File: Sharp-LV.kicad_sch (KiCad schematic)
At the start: 51 parts, among them J1 USB_C_Receptacle_USB2.0, J2 Conn_01x05_PROG, J3 5024260810, J4 FH52-10S-0.5SH_99, J5 SM04B-SRSS-TB_LF__SN_, J6 Conn_2Rows-13Pins, J7 S2B-PH-SM4-TB_LF__SN_, U1 NRF52840-QIAA-R, U2 USBLC6-2P6, U3 MCP1700-3302E_SOT23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

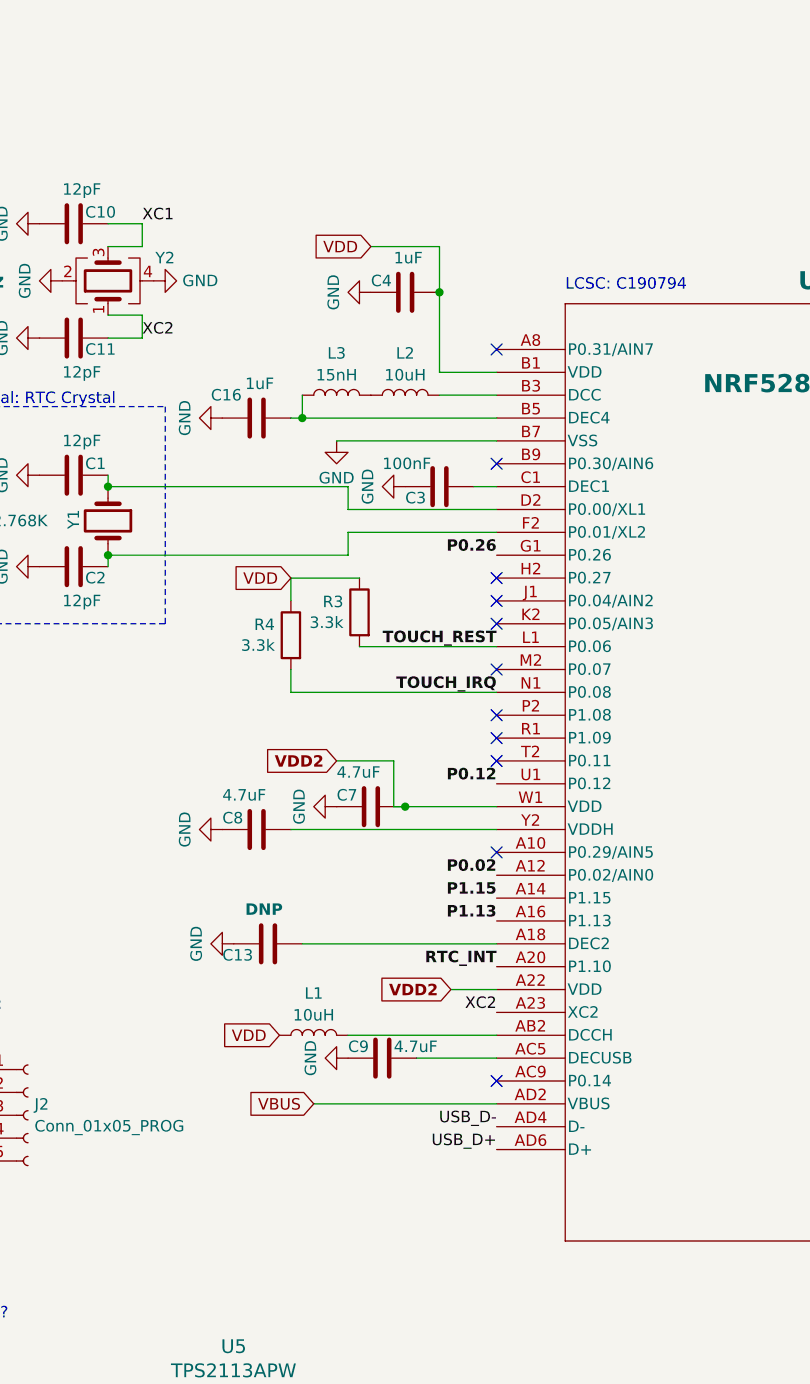
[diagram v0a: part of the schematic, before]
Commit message: Update SCH and add C22 to VUSB
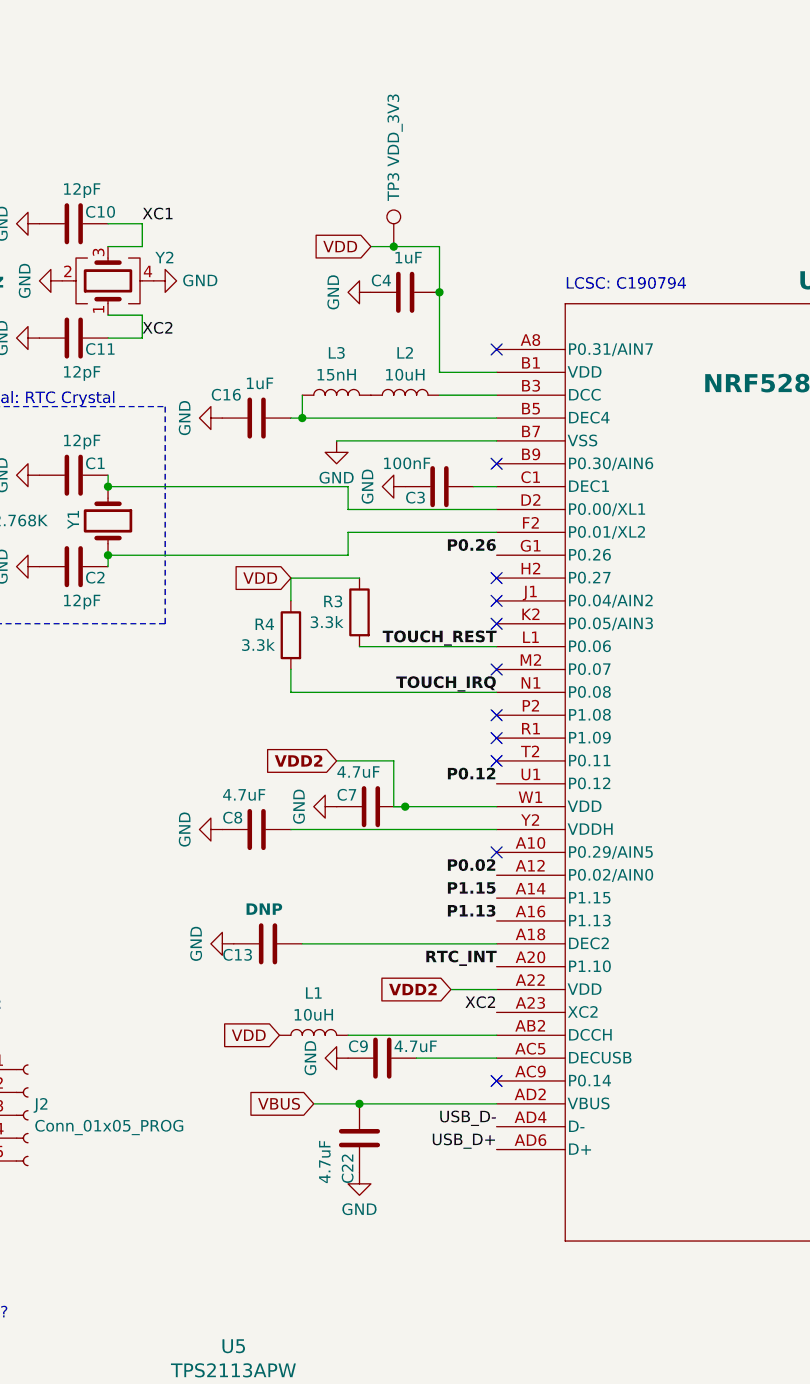
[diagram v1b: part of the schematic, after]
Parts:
- added C22: 4.7uF, Capacitor_SMD:C_0402_1005Metric, symbol Device:C
- added TP3: VDD_3V3, TestPoint:TestPoint_Pad_D1.5mm, symbol Connector:TestPoint
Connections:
- net GND: now also C22.1
- net VBUS: now also C22.2
- net VDD: now also TP3.1
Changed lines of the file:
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@@
   (junction (at 172.72 180.34) (diameter 0) (color 0 0 0 0)
   )
+  (junction (at 168.91 33.02) (diameter 0) (color 0 0 0 0)
+  )
   (junction (at 67.31 58.42) (diameter 0) (color 0 0 0 0)
   )
@@
   (junction (at 67.31 60.96) (diameter 0) (color 0 0 0 0)
   )
+  (junction (at 165.1 128.27) (diameter 0) (color 0 0 0 0)
+  )
   (junction (at 52.07 120.65) (diameter 0) (color 0 0 0 0)
   )
@@
     (stroke (width 0) (type default))
   )
-  (wire (pts (xy 160.02 128.27) (xy 180.34 128.27))
+  (wire (pts (xy 160.02 128.27) (xy 165.1 128.27))
     (stroke (width 0) (type default))
   )
@@
     (stroke (width 0) (type default))
   )
+  (wire (pts (xy 165.1 128.27) (xy 180.34 128.27))
+    (stroke (width 0) (type default))
+  )
   (wire (pts (xy 306.07 184.15) (xy 309.88 184.15))
     (stroke (width 0) (type default))
@@
     (stroke (width 0) (type default))
   )
-  (wire (pts (xy 166.37 33.02) (xy 173.99 33.02))
+  (wire (pts (xy 166.37 33.02) (xy 168.91 33.02))
     (stroke (width 0) (type default))
   )
@@
     (stroke (width 0) (type default))
   )
+  (wire (pts (xy 168.91 33.02) (xy 173.99 33.02))
+    (stroke (width 0) (type default))
+  )
   (wire (pts (xy 180.34 82.55) (xy 157.48 82.55))
     (stroke (width 0) (type default))
@@
     )
   )
+  (symbol (lib_id "Device:C") (at 165.1 132.08 180) (unit 1)
+    (in_bom yes) (on_board yes) (dnp no)
+    (property "Reference" "C22" (at 163.83 137.16 90)
+      (effects (font (size 1.27 1.27)) (justify right))
+    )
+    (property "Value" "4.7uF" (at 161.29 137.16 90)
+      (effects (font (size 1.27 1.27)) (justify right))
+    )
+    (property "Footprint" "Capacitor_SMD:C_0402_1005Metric" (at 164.1348 128.27 0)
+      (effects (font (size 1.27 1.27)) hide)
+    )
+    (property "Datasheet" "~" (at 165.1 132.08 0)
+      (effects (font (size 1.27 1.27)) hide)
+    )
+    (property "LCSC" "C23733" (at 165.1 132.08 0)
+      (effects (font (size 1.27 1.27)) hide)
+    )
+    (pin "1")
+    (pin "2")
+    (instances
+      (project "Sharp-LV"
+        (path "/19808d61-e19c-42f1-b3f4-29e10270d8fb"
+          (reference "C22") (unit 1)
+        )
+      )
+    )
+  )
   (symbol (lib_id "power:GND") (at 170.18 59.69 270) (unit 1)
     (in_bom yes) (on_board yes) (dnp no) (fields_autoplaced)
@@
     )
   )
+  (symbol (lib_id "power:GND") (at 165.1 135.89 0) (unit 1)
+    (in_bom yes) (on_board yes) (dnp no) (fields_autoplaced)
+    (property "Reference" "#PWR042" (at 165.1 142.24 0)
+      (effects (font (size 1.27 1.27)) hide)
+    )
+    (property "Value" "GND" (at 165.1 140.0231 0)
+      (effects (font (size 1.27 1.27)))
+    )
+    (property "Footprint" "" (at 165.1 135.89 0)
+      (effects (font (size 1.27 1.27)) hide)
+    )
+    (property "Datasheet" "" (at 165.1 135.89 0)
+      (effects (font (size 1.27 1.27)) hide)
+    )
+    (pin "1")
+    (instances
+      (project "Sharp-LV"
+        (path "/19808d61-e19c-42f1-b3f4-29e10270d8fb"
+          (reference "#PWR042") (unit 1)
+        )
+      )
+    )
+  )
   (symbol (lib_id "power:GND") (at 162.56 54.61 0) (unit 1)
     (in_bom yes) (on_board yes) (dnp no) (fields_autoplaced)
@@
         )
       )
+    )
+  )
+  (symbol (lib_id "Connector:TestPoint") (at 168.91 33.02 0) (unit 1)
+    (in_bom no) (on_board yes) (dnp no)
+    (property "Reference" "TP3" (at 168.91 27.94 90)
+      (effects (font (size 1.27 1.27)) (justify left))
+    )
+    (property "Value" "VDD_3V3" (at 168.91 24.13 90)
+      (effects (font (size 1.27 1.27)) (justify left))
+    )
+    (property "Footprint" "TestPoint:TestPoint_Pad_D1.5mm" (at 173.99 33.02 0)
+      (effects (font (size 1.27 1.27)) hide)
+    )
+    (property "Datasheet" "~" (at 173.99 33.02 0)
+      (effects (font (size 1.27 1.27)) hide)
+    )
+    (pin "1")
+    (instances
+      (project "Sharp-LV"
+        (path "/19808d61-e19c-42f1-b3f4-29e10270d8fb"
+          (reference "TP3") (unit 1)
+        )
+      )

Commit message: Update SCH & DRC
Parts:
- removed C8: 4.7uF, Capacitor_SMD:C_0402_1005Metric, symbol Device:C
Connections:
- net VDD: now also C7.2, U1.W1 (VDD), U1.Y2 (VDDH)
- net VDD2: no longer C7.2, U1.W1 (VDD)
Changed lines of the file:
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@@
     (stroke (width 0) (type default))
   )
+  (wire (pts (xy 170.18 97.79) (xy 170.18 95.25))
+    (stroke (width 0) (type default))
+  )
   (wire (pts (xy 73.66 120.65) (xy 78.74 120.65))
     (stroke (width 0) (type default))
@@
     (stroke (width 0) (type default))
   )
-  (wire (pts (xy 157.48 97.79) (xy 180.34 97.79))
-    (stroke (width 0) (type default))
-  )
   (wire (pts (xy 278.13 119.38) (xy 278.13 118.11))
     (stroke (width 0) (type default))
@@
     (stroke (width 0) (type default))
   )
-  (wire (pts (xy 168.91 90.17) (xy 168.91 95.25))
+  (wire (pts (xy 170.18 90.17) (xy 170.18 95.25))
     (stroke (width 0) (type default))
   )
@@
     (stroke (width 0) (type default))
   )
-  (wire (pts (xy 162.56 90.17) (xy 168.91 90.17))
+  (wire (pts (xy 157.48 90.17) (xy 170.18 90.17))
     (stroke (width 0) (type default))
   )
@@
     (stroke (width 0) (type default))
   )
-  (wire (pts (xy 168.91 95.25) (xy 170.18 95.25))
+  (wire (pts (xy 180.34 97.79) (xy 170.18 97.79))
     (stroke (width 0) (type default))
   )
@@
     )
   )
-  (global_label "VDD2" (shape input) (at 162.56 90.17 180) (fields_autoplaced)
-    (effects (font (size 1.27 1.27) (thickness 0.254) bold (color 255 0 255 1)) (justify right))
-    (property "Intersheetrefs" "${INTERSHEET_REFS}" (at 154.2607 90.17 0)
-      (effects (font (size 1.27 1.27)) (justify right) hide)
-    )
-    (property "Referenzen zwischen Schaltplänen" "${INTERSHEET_REFS}" (at 162.56 92.456 0)
-      (effects (font (size 1.27 1.27)) (justify right) hide)
-    )
-  )
   (global_label "VDD2" (shape input) (at 175.26 115.57 180) (fields_autoplaced)
     (effects (font (size 1.27 1.27) (thickness 0.254) bold (color 255 0 255 1)) (justify right))
@@
     )
   )
+  (global_label "VDD" (shape input) (at 157.48 90.17 180) (fields_autoplaced)
+    (effects (font (size 1.27 1.27)) (justify right))
+    (property "Intersheetrefs" "${INTERSHEET_REFS}" (at 150.8662 90.17 0)
+      (effects (font (size 1.27 1.27)) (justify right) hide)
+    )
+  )
   (global_label "VDD2" (shape input) (at 256.54 59.69 0) (fields_autoplaced)
     (effects (font (size 1.27 1.27) (thickness 0.254) bold (color 255 0 255 1)) (justify left))
@@
     )
   )
-  (symbol (lib_id "Device:C") (at 153.67 97.79 90) (unit 1)
-    (in_bom yes) (on_board yes) (dnp no)
-    (property "Reference" "C8" (at 149.86 96.52 90)
-      (effects (font (size 1.27 1.27)) (justify right))
-    )
-    (property "Value" "4.7uF" (at 149.86 93.98 90)
-      (effects (font (size 1.27 1.27)) (justify right))
-    )
-    (property "Footprint" "Capacitor_SMD:C_0402_1005Metric" (at 157.48 96.8248 0)
-      (effects (font (size 1.27 1.27)) hide)
-    )
-    (property "Datasheet" "~" (at 153.67 97.79 0)
-      (effects (font (size 1.27 1.27)) hide)
-    )
-    (property "LCSC" "C23733" (at 153.67 97.79 0)
-      (effects (font (size 1.27 1.27)) hide)
-    )
-    (pin "1")
-    (pin "2")
-    (instances
-      (project "Sharp-LV"
-        (path "/19808d61-e19c-42f1-b3f4-29e10270d8fb"
-          (reference "C8") (unit 1)
-        )
-      )
-    )
-  )
   (symbol (lib_id "10_FPC:FH52-10S-0.5SH_99_") (at 351.79 55.88 0) (mirror y) (unit 1)
     (in_bom yes) (on_board yes) (dnp no)
@@
         )
       )
-    )
-  )
-  (symbol (lib_id "power:GND") (at 149.86 97.79 270) (unit 1)
-    (in_bom yes) (on_board yes) (dnp no) (fields_autoplaced)
-    (property "Reference" "#PWR013" (at 143.51 97.79 0)
-      (effects (font (size 1.27 1.27)) hide)
-    )
-    (property "Value" "GND" (at 145.7269 97.79 0)
-      (effects (font (size 1.27 1.27)))
-    )
-    (property "Footprint" "" (at 149.86 97.79 0)
-      (effects (font (size 1.27 1.27)) hide)
-    )
-    (property "Datasheet" "" (at 149.86 97.79 0)
-      (effects (font (size 1.27 1.27)) hide)
-    )
-    (pin "1")
-    (instances
-      (project "Sharp-LV"
-        (path "/19808d61-e19c-42f1-b3f4-29e10270d8fb"
-          (reference "#PWR013") (unit 1)
-        )
-      )

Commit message: Add GND pane
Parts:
- added R8: 5.1k, Resistor_SMD:R_0603_1608Metric, symbol Device:R
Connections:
- net GND: now also R8.2
- net at J1.A5 (CC1): now also R8.1
- no-connect marks 37 -> 36
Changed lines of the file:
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@@
   (no_connect (at 251.46 107.95))
   (no_connect (at 351.79 58.42))
-  (no_connect (at 66.04 48.26))
   (no_connect (at 251.46 92.71))
   (no_connect (at 251.46 57.15))
@@
     (stroke (width 0) (type default))
   )
+  (wire (pts (xy 92.71 58.42) (xy 92.71 55.88))
+    (stroke (width 0) (type default))
+  )
   (wire (pts (xy 137.16 58.42) (xy 137.16 59.69))
     (stroke (width 0) (type default))
@@
   )
   (wire (pts (xy 173.99 49.53) (xy 180.34 49.53))
+    (stroke (width 0) (type default))
+  )
+  (wire (pts (xy 66.04 48.26) (xy 92.71 48.26))
     (stroke (width 0) (type default))
   )
@@
     )
   )
+  (symbol (lib_id "Device:R") (at 92.71 52.07 0) (mirror y) (unit 1)
+    (in_bom yes) (on_board yes) (dnp no)
+    (property "Reference" "R8" (at 90.932 50.9016 0)
+      (effects (font (size 1.27 1.27)) (justify left))
+    )
+    (property "Value" "5.1k" (at 90.932 53.213 0)
+      (effects (font (size 1.27 1.27)) (justify left))
+    )
+    (property "Footprint" "Resistor_SMD:R_0603_1608Metric" (at 94.488 52.07 90)
+      (effects (font (size 1.27 1.27)) hide)
+    )
+    (property "Datasheet" "~" (at 92.71 52.07 0)
+      (effects (font (size 1.27 1.27)) hide)
+    )
+    (property "LCSC" "C23186" (at 92.71 52.07 0)
+      (effects (font (size 1.27 1.27)) hide)
+    )
+    (pin "1")
+    (pin "2")
+    (instances
+      (project "Sharp-LV"
+        (path "/19808d61-e19c-42f1-b3f4-29e10270d8fb"
+          (reference "R8") (unit 1)
+        )
+      )
+    )
+  )
   (symbol (lib_id "Device:C") (at 116.84 186.69 0) (mirror y) (unit 1)
     (in_bom yes) (on_board yes) (dnp no)
@@
         )
       )
+    )
+  )
+  (symbol (lib_id "power:GND") (at 92.71 58.42 0) (unit 1)
+    (in_bom yes) (on_board yes) (dnp no)
+    (property "Reference" "#PWR013" (at 92.71 64.77 0)
+      (effects (font (size 1.27 1.27)) hide)
+    )
+    (property "Value" "GND" (at 92.837 62.8142 0)
+      (effects (font (size 1.27 1.27)))
+    )
+    (property "Footprint" "" (at 92.71 58.42 0)
+      (effects (font (size 1.27 1.27)) hide)
+    )
+    (property "Datasheet" "" (at 92.71 58.42 0)
+      (effects (font (size 1.27 1.27)) hide)
+    )
+    (pin "1")
+    (instances
+      (project "Sharp-LV"
+        (path "/19808d61-e19c-42f1-b3f4-29e10270d8fb"
+          (reference "#PWR013") (unit 1)
+        )
+      )

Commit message: Heading for Rel 1.1
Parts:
- J5: footprint Footprints:QWIIC_SM04B-SRSS-TB_LFSN_ -> SM04B-SRSS-TB(LFSN); symbol Qwiic:SM04B-SRSS-TB_LF__SN_ -> QWIIC:SM04B-SRSS-TB_LF__SN_
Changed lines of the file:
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@@
     (effects (font (size 1.27 1.27)) (justify left top))
   )
-  (text_box "Pending TO-DOs\n\n1 Add QWIIC I2C connector\n\n2 Add TP4057 battery charger circuit\n\n3 Or decide if Rel 1.0 should have this\n\n4 IMPORTANT: Double check initial PROG SWDIO/SWCLK\n  connectors"
+  (text_box "Pending TO-DOs\n\n1 Add QWIIC I2C connector\n\n2 Add TP4057 battery charger circuit: TOP PRIO\n\n3 MicroSD?"
     (at -102.87 7.62 0) (size 90.17 52.07)
     (stroke (width 0) (type default))
@@
     )
   )
-  (symbol (lib_id "Qwiic:SM04B-SRSS-TB_LF__SN_") (at 62.23 162.56 0) (unit 1)
-    (in_bom yes) (on_board yes) (dnp no) (fields_autoplaced)
-    (property "Reference" "J5" (at 81.6143 165.735 90)
-      (effects (font (size 1.27 1.27)))
-    )
-    (property "Value" "SM04B-SRSS-TB_LF__SN_" (at 79.1901 165.735 90)
-      (effects (font (size 1.27 1.27)))
-    )
-    (property "Footprint" "Footprints:QWIIC_SM04B-SRSS-TB_LFSN_" (at 78.74 257.48 0)
+  (symbol (lib_id "QWIIC:SM04B-SRSS-TB_LF__SN_") (at 62.23 162.56 0) (unit 1)
+    (in_bom yes) (on_board yes) (dnp no)
+    (property "Reference" "J5" (at 78.232 164.5229 0)
+      (effects (font (size 1.27 1.27)) (justify left))
+    )
+    (property "Value" "SM04B-SRSS-TB_LF__SN_" (at 59.69 179.07 0)
+      (effects (font (size 1.27 1.27)) (justify left))
+    )
+    (property "Footprint" "SM04B-SRSS-TB(LFSN)" (at 78.74 257.48 0)
       (effects (font (size 1.27 1.27)) (justify left top) hide)
     )
